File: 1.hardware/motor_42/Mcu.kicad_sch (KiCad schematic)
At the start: 26 parts, among them U2 STM32F103CBTx, Y1 YSX321SL_12Mhz

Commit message: 얼추 다 그림
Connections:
- net WS2812_SIGNAL: no longer names the net of U2.21 (PB10)
- no-connect marks 9 -> 10
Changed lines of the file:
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@@
+	)
+	(no_connect
+		(at 137.16 116.84)
 	)
 	(no_connect
@@
 	(wire
 		(pts
-			(xy 133.35 116.84) (xy 137.16 116.84)
-		)
-		(stroke
-			(width 0)
-			(type default)
-		)
-	)
-	(wire
-		(pts
 			(xy 157.48 50.8) (xy 157.48 55.88)
 		)
@@
 			(effects
 				(font
-					(size 1.27 1.27)
-				)
-				(justify right)
-				(hide yes)
-			)
-		)
-	)
-	(global_label "WS2812_SIGNAL"
-		(shape passive)
-		(at 133.35 116.84 180)
-		(fields_autoplaced yes)
-		(effects
-			(font
-				(size 1.27 1.27)
-			)
-			(justify right)
-		)
-		(property "Intersheetrefs" "${INTERSHEET_REFS}"
-			(at 116.4781 116.84 0)
-			(effects
-				(font

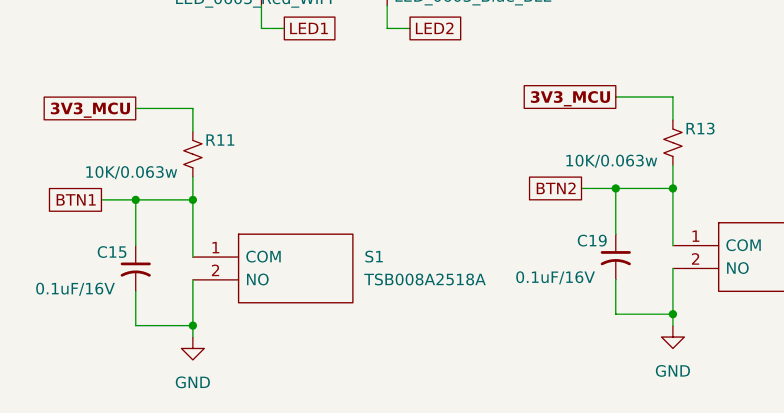
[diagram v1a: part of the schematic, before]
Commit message: 비아 변경 필요
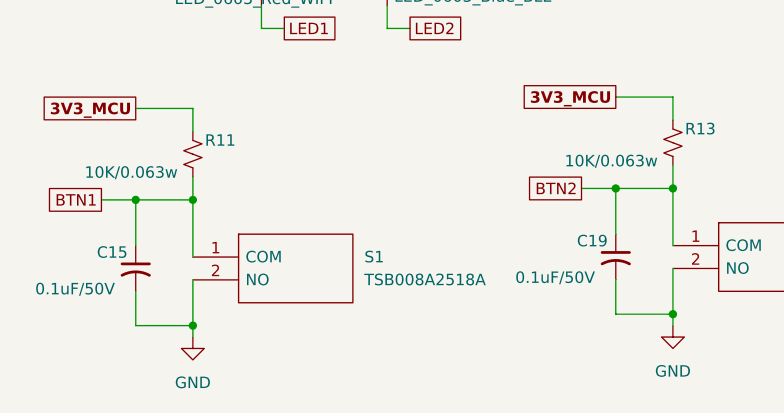
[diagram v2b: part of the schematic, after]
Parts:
- C15, C19: value 0.1uF/16V -> 0.1uF/50V
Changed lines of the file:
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@@
 			)
 		)
-		(property "Value" "0.1uF/16V"
+		(property "Value" "0.1uF/50V"
 			(at 77.724 153.416 0)
 			(effects
@@
 			)
 		)
-		(property "Value" "0.1uF/16V"
+		(property "Value" "0.1uF/50V"
 			(at 24.384 154.686 0)
 			(effects

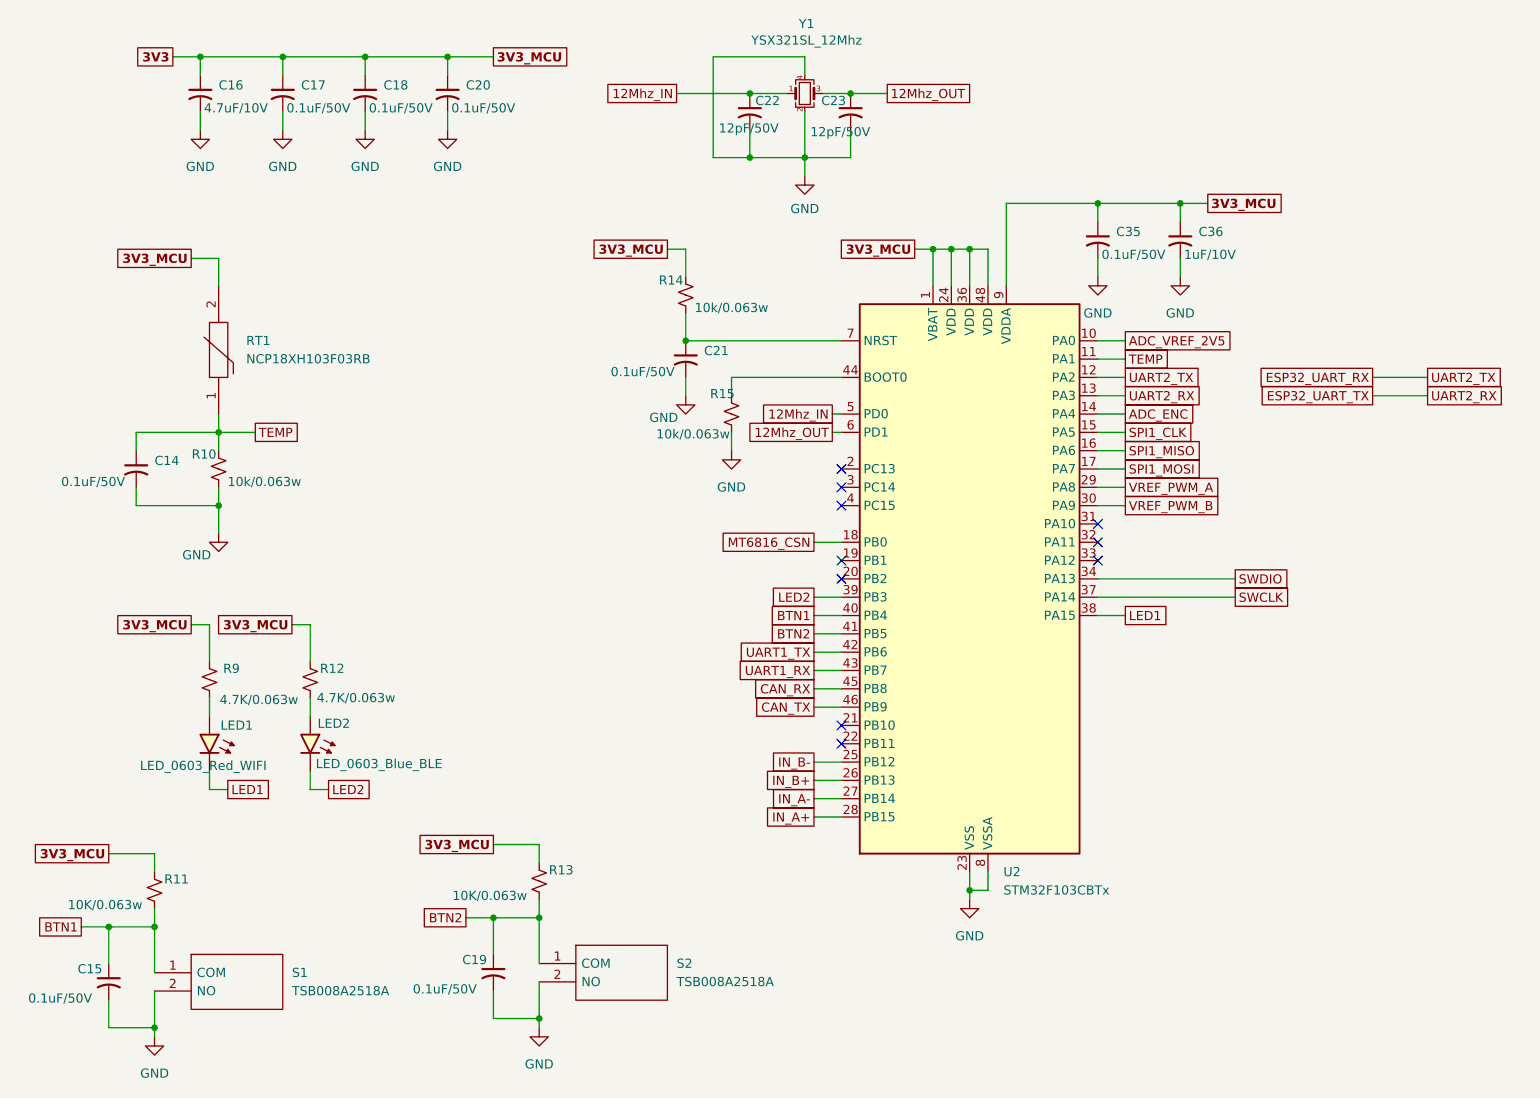
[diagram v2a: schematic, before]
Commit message: 번호 초기화 및 led 변경
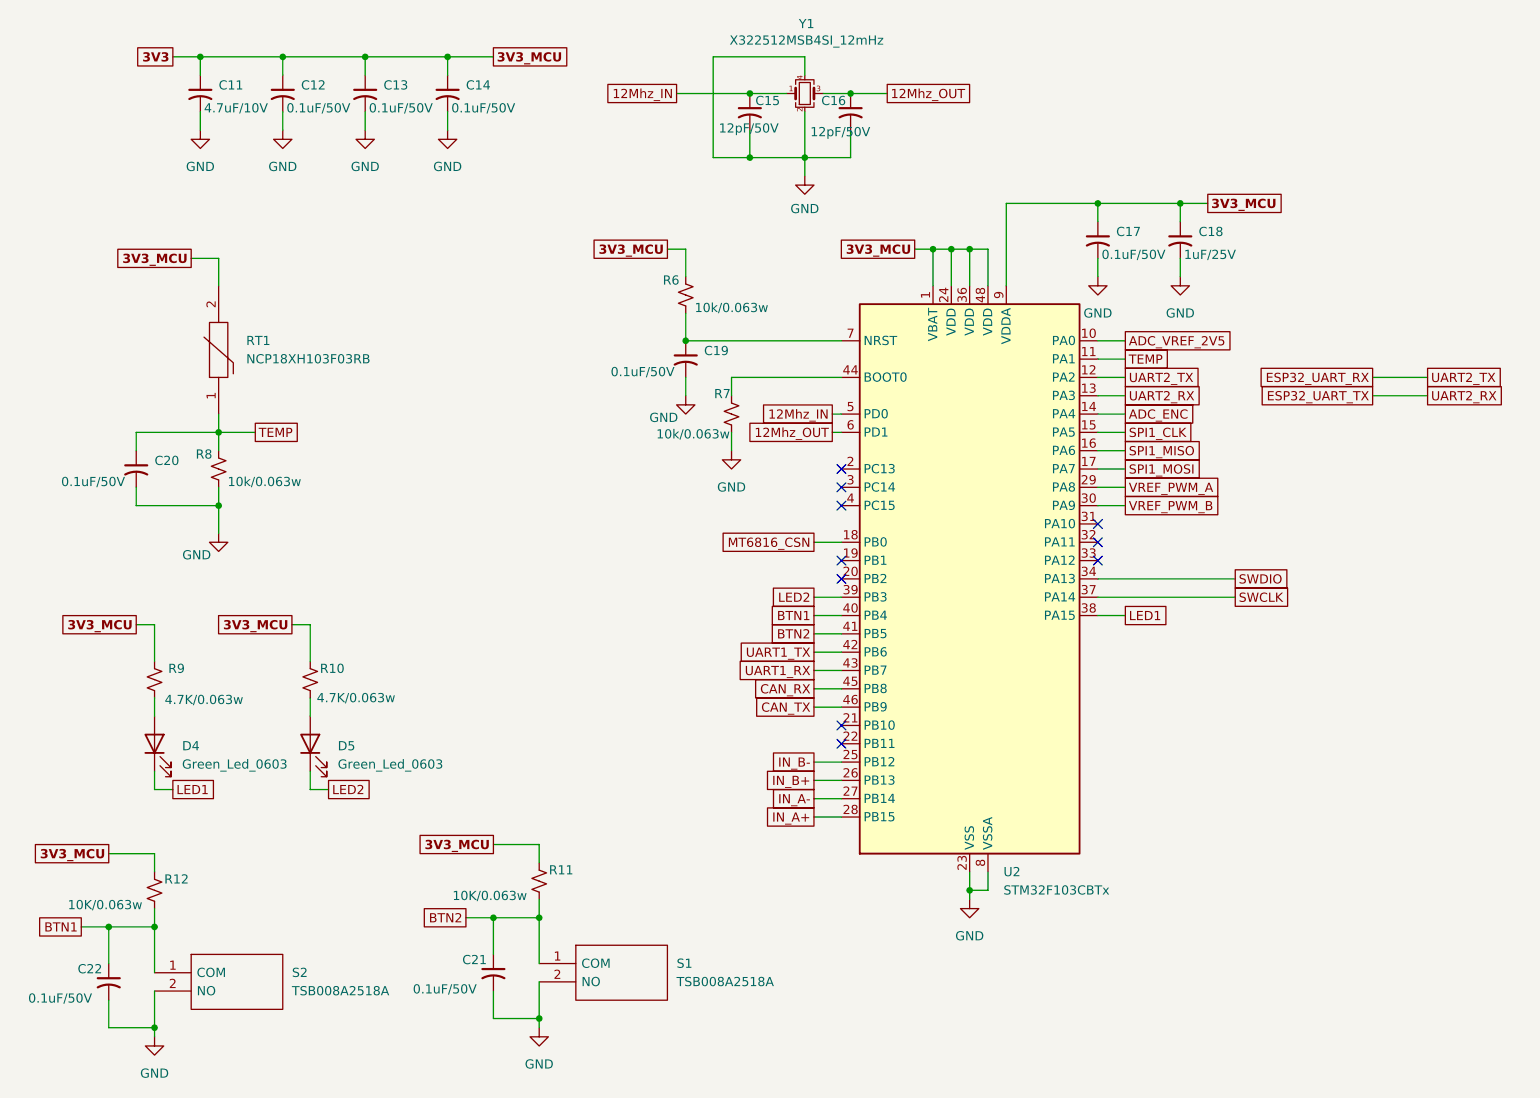
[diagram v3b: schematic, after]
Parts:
- removed LED1: LED_0603_Red_WIFI, PCM_LED_SMD_AKL:LED_0603_1608Metric, symbol PCM_LED_AKL:LED_0603_Red
- removed LED2: LED_0603_Blue_BLE, PCM_LED_SMD_AKL:LED_0603_1608Metric, symbol PCM_LED_AKL:LED_0603_Blue
- added D4, D5: Green_Led_0603, LED_SMD:LED_0603_1608Metric, symbol Device:LED
- C18: renamed from C36; value 1uF/10V -> 1uF/25V
- Y1: value YSX321SL_12Mhz -> X322512MSB4SI_12mHz
- renumbered C16 to C11, C17 to C12, C18 to C13, C20 to C14, C22 to C15, C23 to C16, C35 to C17, C21 to C19, C14 to C20, C19 to C21, C15 to C22, R12 to R10, R13 to R11, R11 to R12, R14 to R6, R15 to R7, R10 to R8, S2 to S1, S1 to S2
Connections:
- net LED1: now also D4.1 (K)
- net LED2: now also D5.1 (K)
- net at R9.2: now also D4.2 (A)
- net at R10.2: now also D5.2 (A)
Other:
- moved on the sheet: R9
